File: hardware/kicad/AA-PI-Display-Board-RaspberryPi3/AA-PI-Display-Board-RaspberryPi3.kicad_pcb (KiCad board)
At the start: 2 copper layers, 140 x 85 mm, 111 parts, among them J1 CTP Interface, J10 MCU Interface, J11 NTC Thermistor, J12 Battery, J2 USB_B_Micro, J3 USB_B_Mini, J4 Wall adapter, J5 MCU Power, J6 LCD Interface, J7 Power Status, J8 RaspberryPi MIPI-DSI Interface, J9 VNA Board Interface, Q1 IRLML6244, Q2 IRLML2244, Q3 IRLML6244, Q4 IRLML2244, Q5 IRLML2244, Q6 IRLML2244, Q7 IRLML6244, Q8 IRLML2244, SW1 SW_SPST, SW2 SW_SPDT, U1 LTC4412, U2 AMS1117-3.3, U3 WM8731, U4 MCP73833, U5 TPS61030PWP, U6 FAN5333BSX, Y1 12.288M

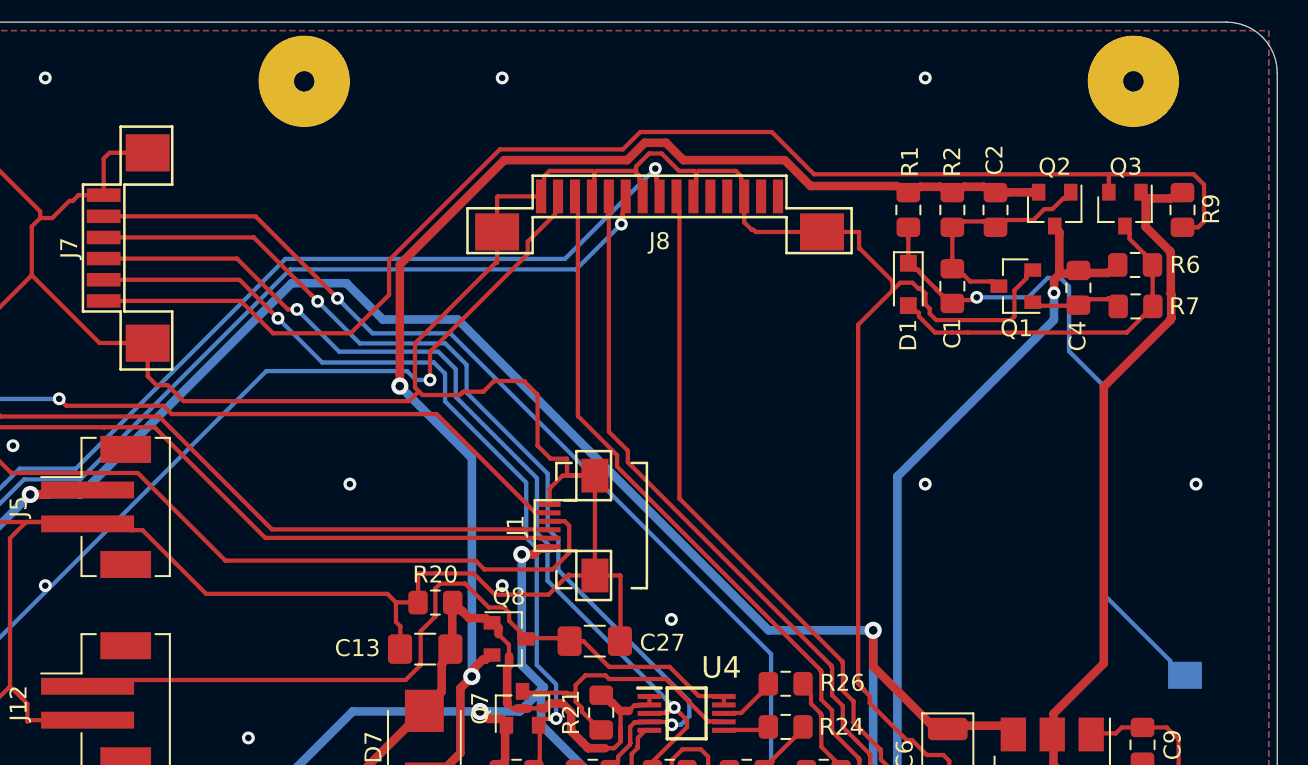
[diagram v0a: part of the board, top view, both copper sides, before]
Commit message: Rotated DSI connector to match RPI orientation
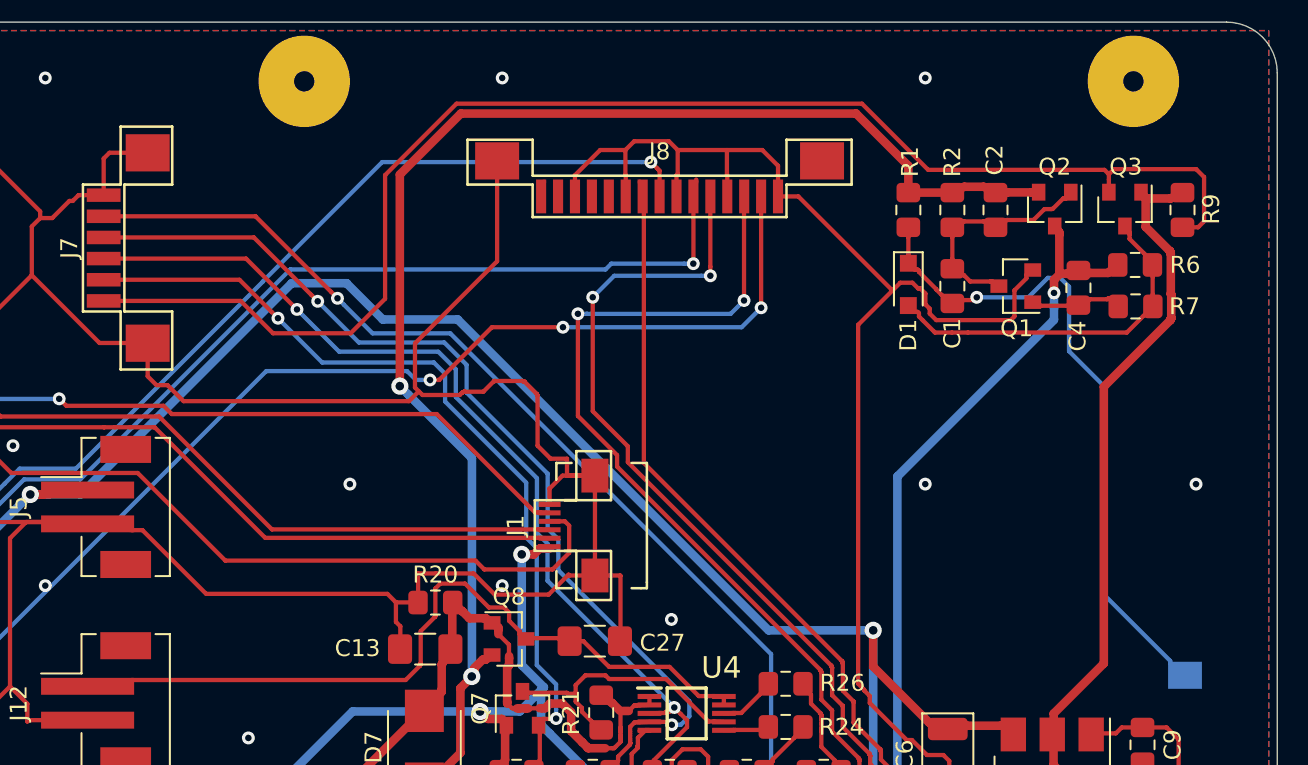
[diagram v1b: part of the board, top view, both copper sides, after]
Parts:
- turned J8 to 180 degrees
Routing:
- net DSI_D1_N: track 93.2 -> 107.2 mm, vias 2 -> 4
- net DSI_D1_P: track 174.7 -> 184.7 mm, vias 0 -> 2
- net DSI_CLK_N: track 176.7 -> 183.4 mm, vias 0 -> 2
- net DSI_CLK_P: track 98.8 -> 105.4 mm
- net V_SW: track 77.9 -> 83.3 mm
- net SHDN_CTRL: track 77.9 -> 82.9 mm
- net DSI_D0_P: track 187.6 -> 189.4 mm
- net Net-(J8-Pad15): track 0.00 -> 0.89 mm
- net GND: track 888.0 -> 888.5 mm

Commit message: planned update (hardware)
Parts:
- removed REF**: KiCad-Logo2_6mm_SilkScreen, Symbol:KiCad-Logo2_6mm_SilkScreen
- added C28: 2.2u, AA-PI-Footprints:C_1206_3216Metric_Pad1.42x1.75mm_HandSolder, F.Cu at (89.3, 66.2)
- added C29: 22n, AA-PI-Footprints:C_0805_2012Metric_Pad1.15x1.40mm_HandSolder, F.Cu at (83.8, 62.1)
- added C30: 10u, AA-PI-Footprints:C_1206_3216Metric_Pad1.42x1.75mm_HandSolder, F.Cu at (79.8, 64.9)
- added C31: 100n, AA-PI-Footprints:C_0805_2012Metric_Pad1.15x1.40mm_HandSolder, F.Cu at (212.0, 79.1)
- added C32: 10u, AA-PI-Footprints:CP_EIA-3528-21_Kemet-B, F.Cu at (201.8, 73.9)
- added Q10: IRLML6244, AA-PI-Footprints:SOT-23, F.Cu at (212.3, 81.8)
- added Q9: IRLML6244, AA-PI-Footprints:SOT-23, F.Cu at (215.9, 78.4)
- added R31: 75K, AA-PI-Footprints:R_0805_2012Metric_Pad1.15x1.40mm_HandSolder, F.Cu at (88.3, 62.1)
- added R32: 0, AA-PI-Footprints:R_0805_2012Metric_Pad1.15x1.40mm_HandSolder, F.Cu at (93.2, 63.7)
- added R33: 10K, AA-PI-Footprints:R_0805_2012Metric_Pad1.15x1.40mm_HandSolder, F.Cu at (214.0, 75.6)
- added R34: 10K, AA-PI-Footprints:R_0805_2012Metric_Pad1.15x1.40mm_HandSolder, F.Cu at (208.6, 81.0)
- added R35: 500K, AA-PI-Footprints:R_0805_2012Metric_Pad1.15x1.40mm_HandSolder, F.Cu at (204.8, 82.5)
- added R36: 380K, AA-PI-Footprints:R_0805_2012Metric_Pad1.15x1.40mm_HandSolder, F.Cu at (208.2, 79.1)
- added RV1: 200K, AA-PI-Footprints:SMD-Potentiometer-Trimmer-B6W-3x3T, F.Cu at (204.7, 79.3)
- added U7: RT9193-2HPB, SOT94P279X130-5N, F.Cu at (83.8, 65.5)
- added U8: MCP3421A0T-E_CH, AA-PI-Footprints:SOT95P280X100-6N, F.Cu at (210.0, 76.4)
- C22, C23: value 22p -> 18p
- R14, R15: value - -> void
- U6: value FAN5333BSX -> FAN5333B
- moved C26 0.49 mm to (72.1, 68.1)
- moved CH1 0.40 mm to (178.2, 84.5)
- moved C21 0.39 mm to (74.8, 68.1)
- moved L2 0.26 mm to (64.6, 75.0)
- moved R29 0.12 mm to (158.7, 106.3)
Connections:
- net Net-(C27-Pad1) renamed V_BATT
- J10 pad 7: Net-(J10-Pad7) -> ADC_EN
- J10 pad 8: Net-(J10-Pad8) -> RADIO_EN
- J11 pad MP: GND -> (no net)
- J12 pad MP: GND -> (no net)
- J5 pad MP: GND -> (no net)
- J9 pad 3: I2C_SDA -> I2C_SCL
- J9 pad 4: I2C_SCL -> I2C_SDA
- J9 pad 6: Net-(J9-Pad6) -> RADIO_EN
- L2 pad 1: +3V3 -> V_ADC
- L3 pad 1: +3V3 -> V_ADC
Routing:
- net RADIO_EN: track 0.00 -> 59.5 mm
- net +5V: track 170.5 -> 230.0 mm, vias 4 -> 5
- net +3V3: track 287.3 -> 231.5 mm
- net ADC_EN: track 0.00 -> 35.0 mm, vias 0 -> 2
- net V_ADC: track 0.00 -> 23.1 mm, vias 0 -> 2
- net GND: track 888.5 -> 877.8 mm, vias 26 -> 35
- net I2C_SCL: track 124.5 -> 127.2 mm
- net Net-(C29-Pad1): track 0.00 -> 2.62 mm
- net PWM_MCU: track 18.7 -> 20.1 mm
- net I2C_SDA: track 127.0 -> 127.9 mm
- net LCD_RESET: track 112.7 -> 113.4 mm
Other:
- board text added: "(C) 2013-2019 ORPALTECH AA-PI Version 2.1"
- board text removed: "(C) 2018 ORPALTECH AA-PI Version 2.0"
